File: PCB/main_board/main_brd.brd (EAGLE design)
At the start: 104.1 x 127 mm, 29 parts, among them J1 MS5803_14BA Break_out, J2 SD-card Adapter, J3 E-paper Module, J4 Zigbee Module, J5 BATT, J6 CHARGER, J7 POGO_PINS, J8 ST-LINK, U1 STM32F103C8T6-MODULE

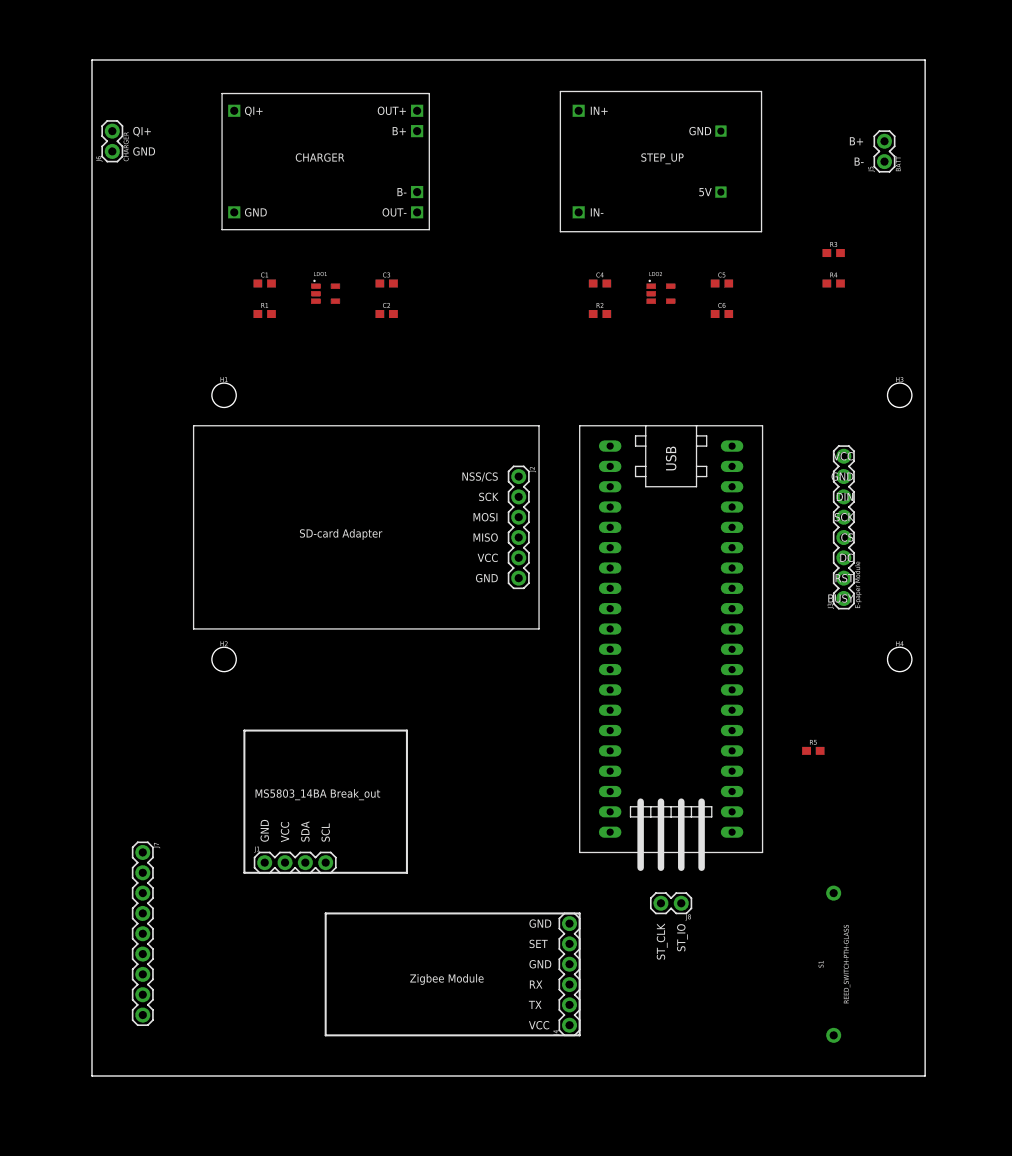
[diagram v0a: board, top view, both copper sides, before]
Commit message: added I2C bus to the schematic and did the routing for the PCB board
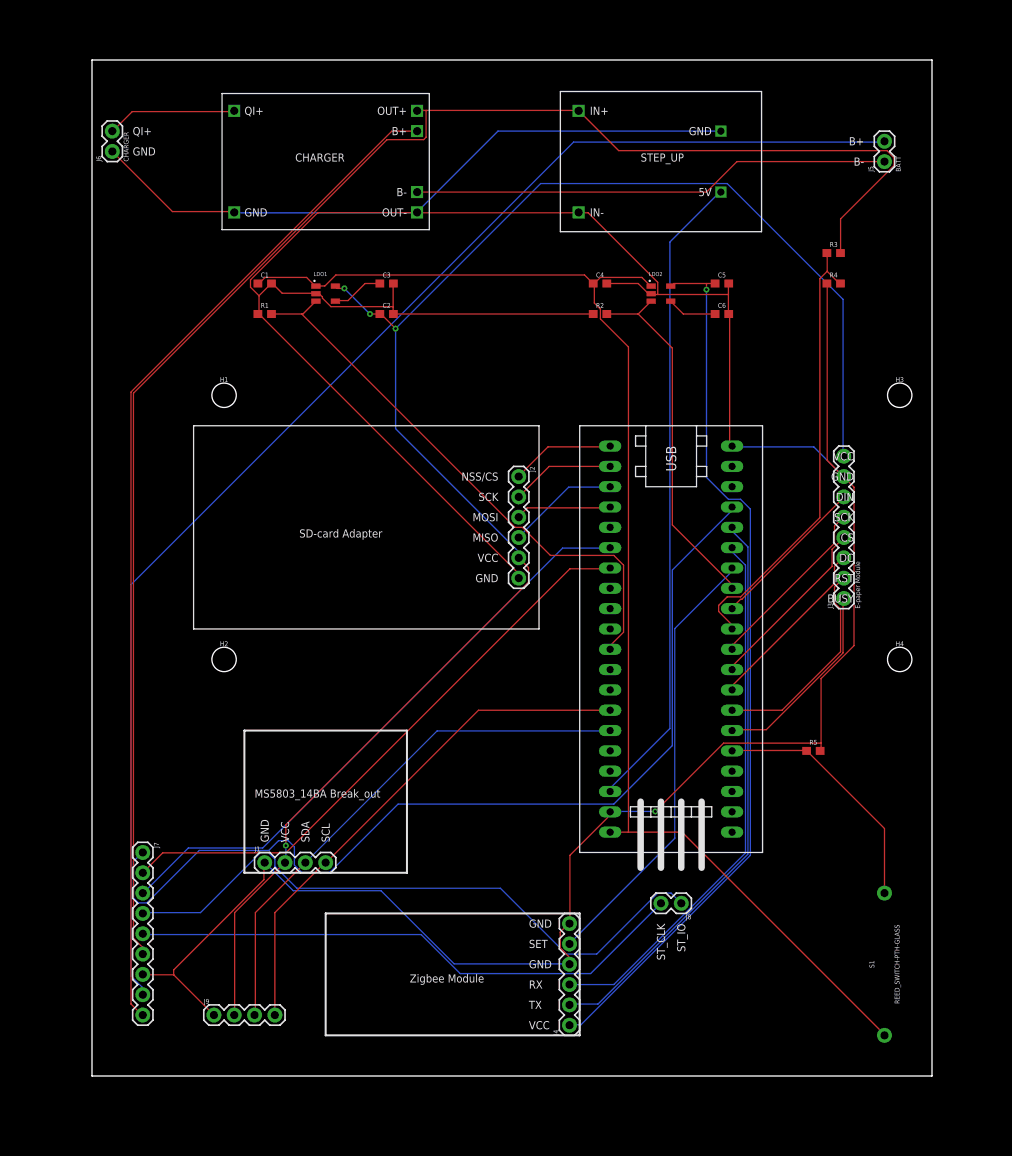
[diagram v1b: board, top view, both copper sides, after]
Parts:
- added J9: additional I2C bus, SparkFun-Connectors:1X04
- moved S1 6.35 mm to (99.1, 14.0)
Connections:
- net GND: now also J9.1
- net I2C_SCL: now also J9.4
- net I2C_SDA: now also J9.3
- net LDO1_3.3V: now also J9.2
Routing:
- net GND: track 0.00 -> 480.9 mm, vias 0 -> 1
- net LDO1_3.3V: track 0.00 -> 206.9 mm, vias 0 -> 4
- net V_CHARGE: track 0.00 -> 200.6 mm
- net B+1: track 0.00 -> 169.1 mm
- net 3.3V: track 0.00 -> 166.9 mm
- net B+0: track 0.00 -> 127.8 mm
- net RST: track 0.00 -> 119.5 mm
- net LDO2_3.3V: track 0.00 -> 111.7 mm, vias 0 -> 1
- net 5V: track 0.00 -> 80.7 mm
- net ST_IO: track 0.00 -> 79.9 mm
- net TX: track 0.00 -> 76.3 mm
- net RX: track 0.00 -> 74.3 mm
- net ZIGBEE_TX: track 0.00 -> 71.8 mm
- net LDO1_EN: track 0.00 -> 70.7 mm
- net ST_CLK: track 0.00 -> 70.5 mm
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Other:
- board size 104.1 x 127 mm -> 105 x 127 mm

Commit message: updated board
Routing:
- net V_CHARGE: track 200.6 -> 209.1 mm
- net LDO2_3.3V: track 111.7 -> 117.7 mm
- net B+0: track 127.8 -> 131.8 mm
- net ZIGBEE_TX: track 71.8 -> 75.2 mm
- net ZIGBEE_RX: track 67.7 -> 69.1 mm
- net E-INK_RST: track 26.6 -> 25.4 mm
- net RST: track 119.5 -> 120.4 mm
- net GND: track 480.9 -> 481.5 mm

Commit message: finalized PCB and updated the Voltage reading methodology
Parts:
- added C8: UWT1C221MCL1GSU2-K-M, capacitor_220uF:U2-K-M
- added TP1, TP2, TP3, TP4, TP5, TP6, TP7, TP8: TEST-POINT3X5, SparkFun-Connectors:PAD.03X.05
- moved C2 4.03 mm to (34.8, 98.8)
- moved C3 3.20 mm to (34.8, 96.6)
- moved C6 2.69 mm to (76.2, 96.2)
- moved R1 2.69 mm to (24.1, 96.2)
- moved R2 2.69 mm to (66.0, 96.2)
- moved C1 2.55 mm to (24.1, 98.6), turned to 180 degrees
- moved C4 2.50 mm to (66.0, 99.1), turned to 180 degrees
- moved C5 2.50 mm to (76.2, 99.1)
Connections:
- removed net 5V: U$2.5V, U1.5V
- new net +5V: C1.1, C4.1, LDO1.1, LDO2.1, TP1.P$1, U$2.5V, U1.5V
- net 3.3V: no longer C1.1, C4.1, LDO1.1, LDO2.1
- net GND: now also C8.2
- net I2C_SCL: now also TP3.P$1
- net I2C_SDA: now also TP2.P$1
- net LDO1_3.3V: now also TP4.P$1
- net LDO1_EN: now also U1.PB_0; no longer U1.PB_3
- net LDO2_3.3V: now also TP5.P$1
- net LDO2_EN: now also U1.PB_3; no longer U1.PB_0
- net SPI1_MOSI: now also TP6.P$1
- net SPI1_NSS/CS: now also TP8.P$1
- net SPI1_SCK: now also TP7.P$1
- net V_CHARGE: now also C8.1
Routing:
- net GND: track 481.5 -> 0.00 mm, vias 1 -> 0
- net +5V: track 0.00 -> 144.2 mm, vias 0 -> 1
- net 3.3V: track 166.9 -> 48.8 mm
- net 5V: track 80.7 -> 0.00 mm
- net LDO1_3.3V: track 206.8 -> 167.5 mm, vias 4 -> 0
- net RST: track 120.4 -> 91.6 mm
- net LDO1_EN: track 70.7 -> 92.1 mm, vias 0 -> 1
- net B+1: track 169.1 -> 148.8 mm, vias 0 -> 2
- net V_CHARGE: track 209.1 -> 189.6 mm, vias 0 -> 1
- net ST_IO: track 79.9 -> 69.1 mm
- net I2C_SCL: track 65.2 -> 74.6 mm
- net SPI1_NSS/CS: track 22.3 -> 31.6 mm
- net TX: track 76.3 -> 83.6 mm
- net SPI1_MOSI: track 20.4 -> 27.5 mm
- net ZIGBEE_TX: track 75.2 -> 68.9 mm, vias 0 -> 1
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- added copper zone on layer 1, net GND
- added copper zone on layer 16, net GND
